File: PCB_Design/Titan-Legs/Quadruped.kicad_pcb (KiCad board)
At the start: 4 copper layers, 55.5 x 55.5 mm, 85 parts, among them IC1 TPS54260DGQR, IC2 CP2102, IC3 DRV8323RSRGZT, J1 TYPE-C-31-M-12, J2 691214110003, P1 282837-2, P2 282837-2, Q1 BSC031N06NS3GATMA1, Q2 BSC031N06NS3GATMA1, Q3 BSC031N06NS3GATMA1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

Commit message: Added Changes after First Review
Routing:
- net /DRV8323/MOTOR_A: track 27.0 -> 28.2 mm
- net Net-(C31-Pad2): track 21.4 -> 22.6 mm
- net /IO20: track 35.1 -> 34.1 mm
- net /DRV8323/SPB: track 19.2 -> 18.2 mm
- net /DRV8323/GLB: track 22.0 -> 22.9 mm
- net /IO8: track 26.9 -> 27.6 mm
- net /DRV8323/SPA: track 54.0 -> 53.6 mm, vias 3 -> 2
- net VM: vias 44 -> 69
- net GND: vias 46 -> 91
- added copper zone on B.Cu, net GND

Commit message: Added Changes after First Review
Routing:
- net VM: track 46.3 -> 52.2 mm, vias 69 -> 129
- net /RTS: track 54.8 -> 55.3 mm
- net GND: vias 91 -> 83
- added copper zone on In2.Cu, net /DRV8323/MOTOR_A
- added copper zone on In2.Cu, net /DRV8323/MOTOR_B
- added copper zone on In2.Cu, net /DRV8323/MOTOR_C

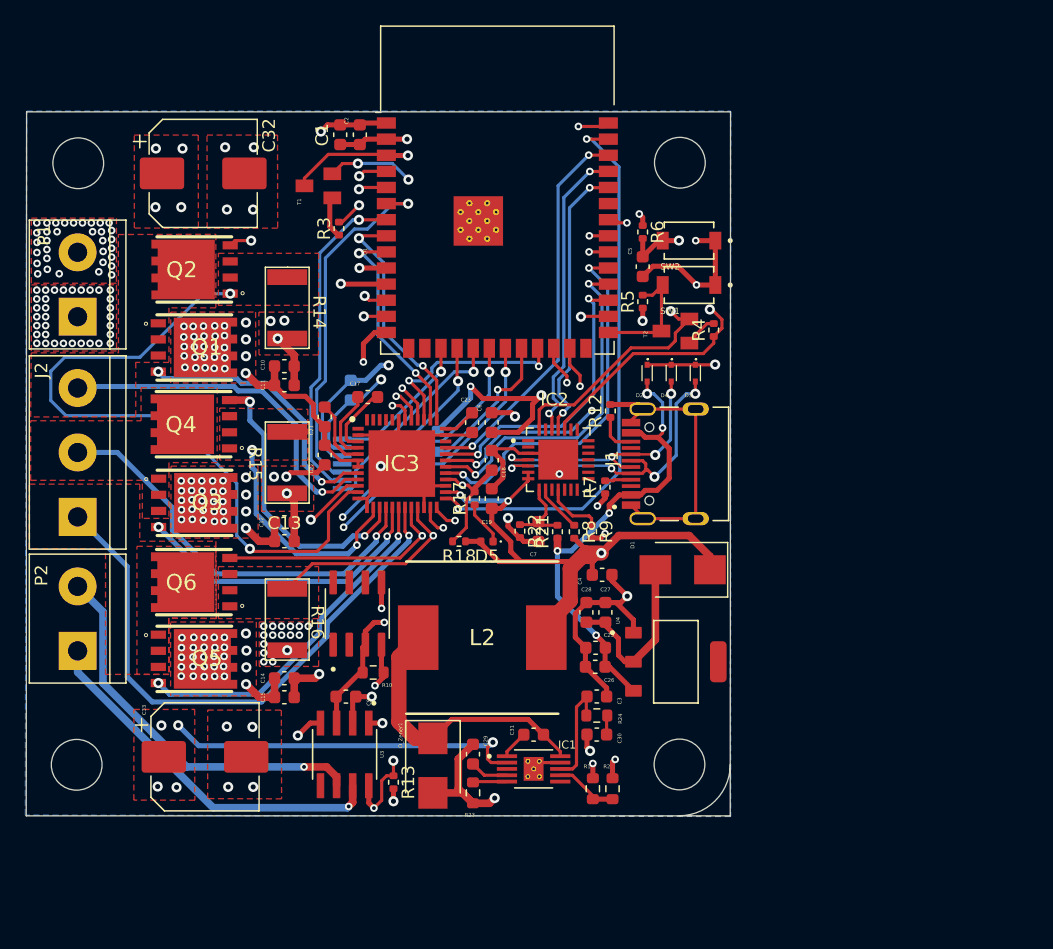
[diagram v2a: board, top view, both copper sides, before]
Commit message: Merged silkscreen changes and completed final prototype
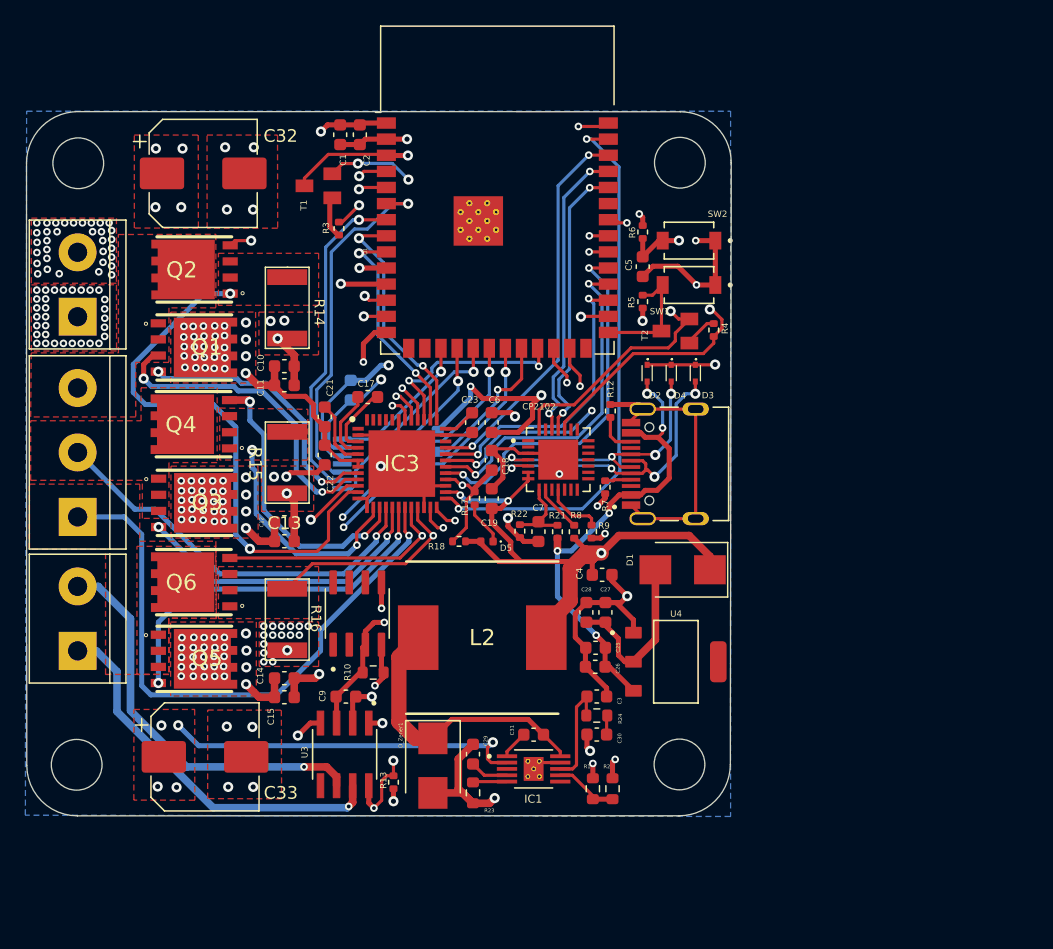
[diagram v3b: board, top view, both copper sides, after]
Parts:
- added G***: LOGO, LOGO, B.Cu at (64.5, 116.2)
- added G***: LOGO, LOGO, B.Cu at (64.1, 121.8)
- added G***: LOGO, LOGO, B.Cu at (47.6, 89.0)
- added G***: LOGO, LOGO, B.Cu at (70.1, 89.0)
- renumbered IC2 to CP2102
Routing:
- net /DRV8323/SPA: track 53.8 -> 43.3 mm
- net /DRV8323/MOTOR_A: track 28.2 -> 25.7 mm, vias 1 -> 2
- net /DRV8323/MOTOR_C: track 45.9 -> 47.7 mm
- net /DRV8323/GHC: track 27.6 -> 29.0 mm
- net /DRV8323/MOTOR_B: track 32.7 -> 31.6 mm
- net /CAN_BUS_IC/CANL: track 30.6 -> 31.6 mm
- net /CAN_BUS_IC/CANH: track 29.3 -> 30.2 mm
- net /IO4: track 40.8 -> 40.0 mm
- net /IO5: track 38.5 -> 37.7 mm
- net /DRV8323/GLA: track 31.1 -> 31.7 mm
- net VM: vias 129 -> 127
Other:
- board size 55.5 x 55.5 mm -> 55.6 x 55.5 mm
- board text added: "&"
- board text added: "Designed by"

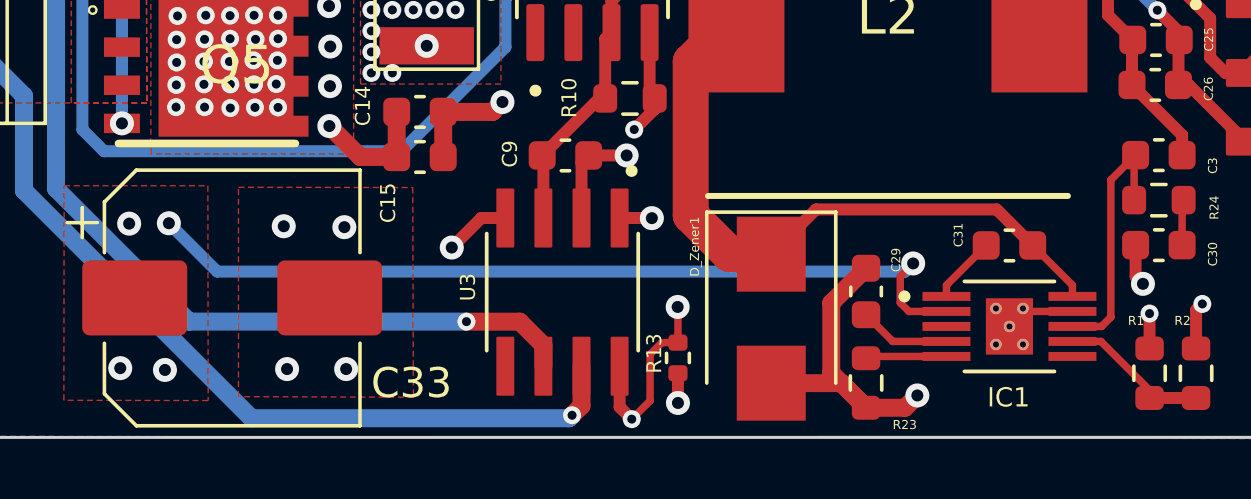
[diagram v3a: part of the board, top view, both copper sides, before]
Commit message: removed unnecessary files
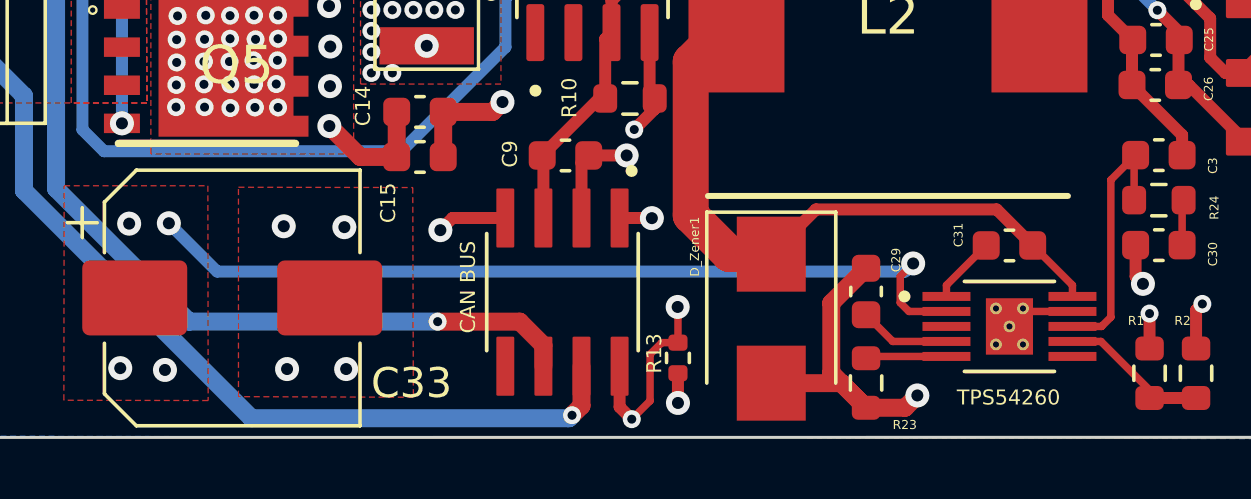
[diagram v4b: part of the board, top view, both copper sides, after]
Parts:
- CAN BUS: renamed from U3
- renumbered IC1 to TPS54260

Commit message: Merged the silkscreen MA,MB,MC and added vias in shunt resistors
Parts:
- removed C18: 0.1uF, Capacitor_SMD:C_0603_1608Metric
- added G***: LOGO, LOGO, B.Cu at (30.1, 97.2)
- added G***: LOGO, LOGO, B.Cu at (30.0, 102.3)
- added G***: LOGO, LOGO, B.Cu at (30.0, 112.9)
- added G***: LOGO, LOGO, B.Cu at (30.1, 107.2)
- added G***: LOGO, LOGO, B.Cu at (30.1, 117.8)
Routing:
- net GND: track 158.2 -> 151.6 mm, vias 83 -> 94
- net /IO47: track 26.7 -> 24.4 mm

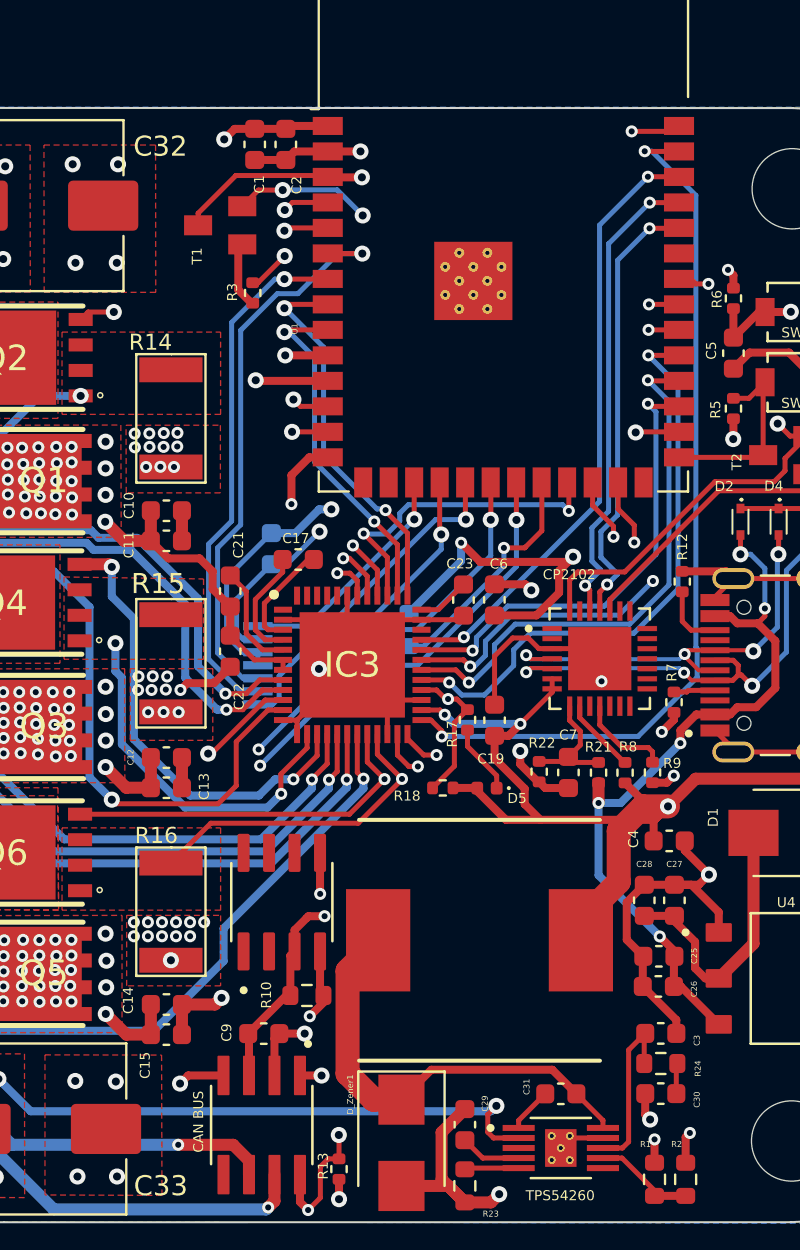
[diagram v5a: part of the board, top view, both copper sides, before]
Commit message: Merged the silkscreen MA,MB,MC and added more vias in shunt resistors
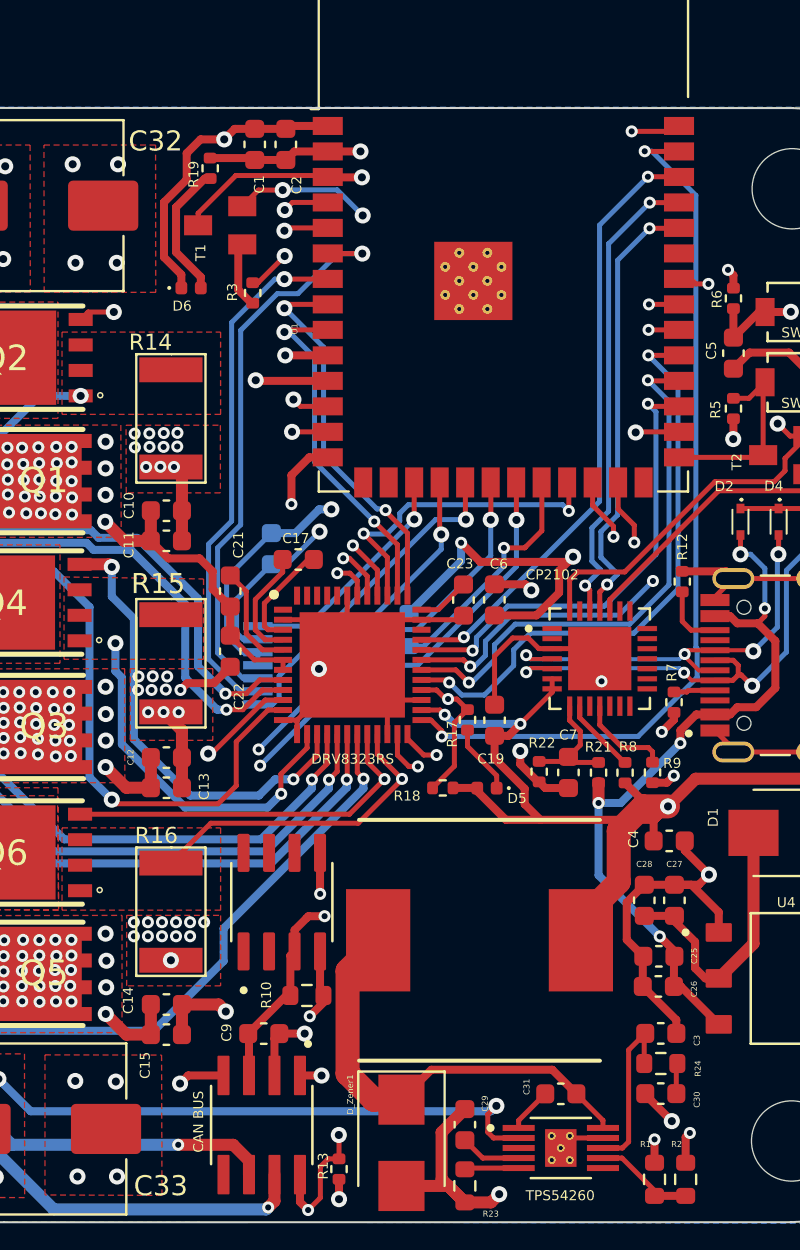
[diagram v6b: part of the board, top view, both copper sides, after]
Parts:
- added D6: LED, LED_SMD:LED_0402_1005Metric, F.Cu at (50.3, 84.3)
- added R19: 330, Resistor_SMD:R_0402_1005Metric, F.Cu at (51.3, 78.3)
- renumbered IC3 to DRV8323RS
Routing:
- net GND: track 151.6 -> 167.0 mm
- net Net-(D6-Pad2): track 0.00 -> 6.82 mm
- net 3V3_IN: track 98.5 -> 100.7 mm

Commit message: Added JLCPCB Logo on Back Silkscreen and final Changes Merged
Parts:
- added G***: LOGO, LOGO, B.Cu at (45.7, 79.8)
- moved G*** 20.6 mm to (66.0, 79.7)
- moved G*** 13.9 mm to (56.5, 91.3)
- moved G*** 0.92 mm to (64.8, 121.2)
- moved G*** 0.42 mm to (64.8, 116.0)

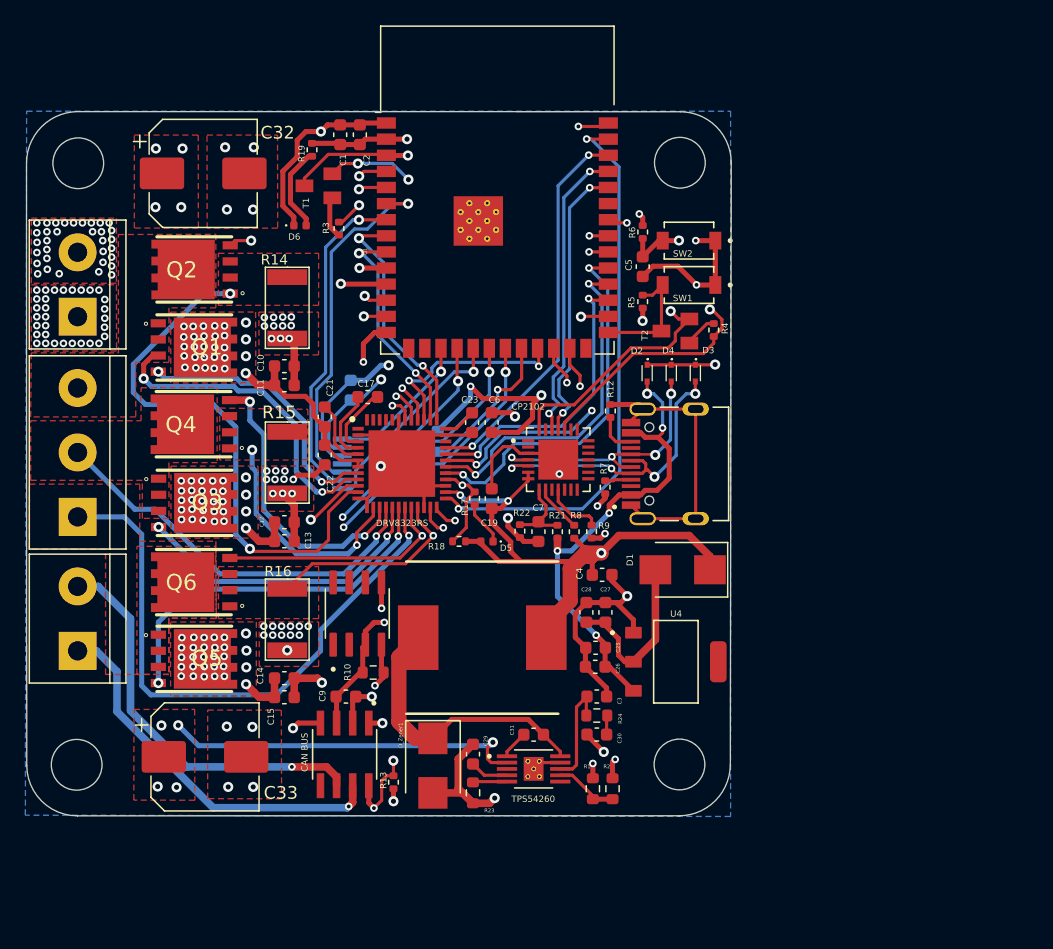
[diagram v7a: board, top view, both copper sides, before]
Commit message: Added Electrolytic Capacitor for TPS54260 and resisotrs for EN pin
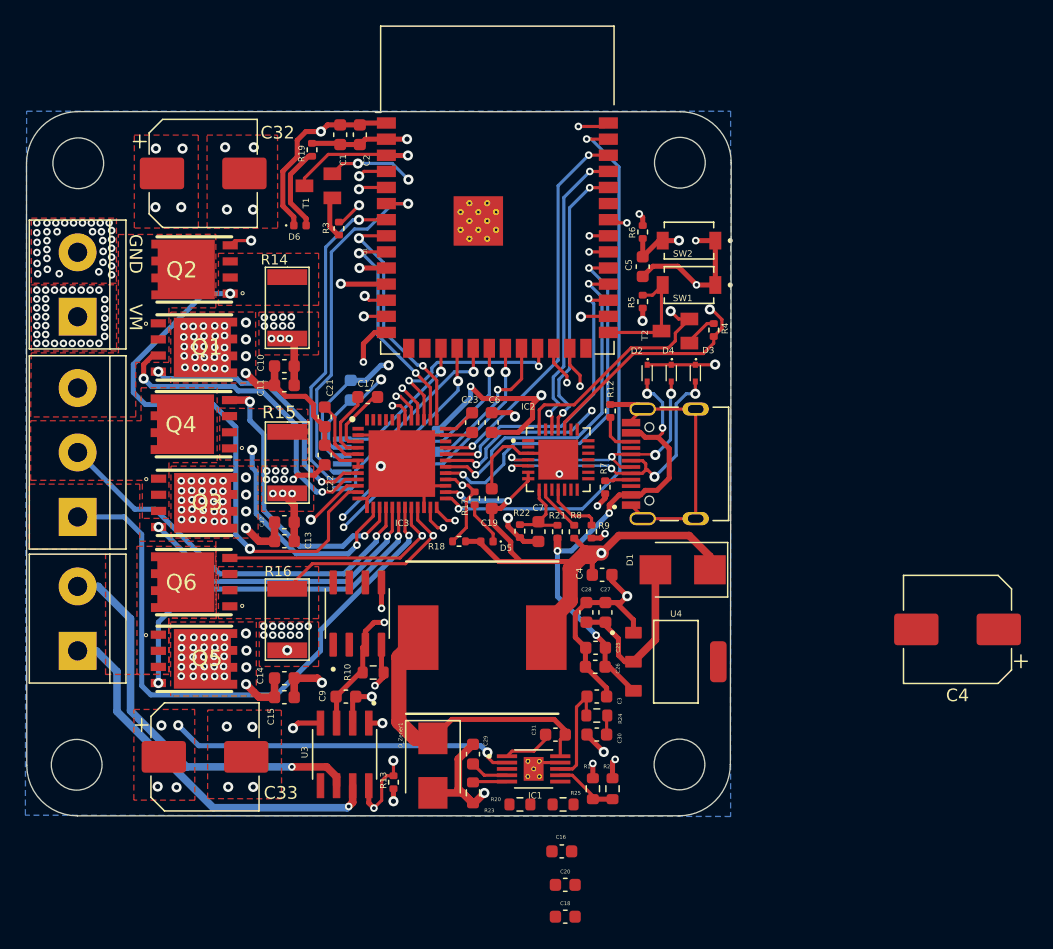
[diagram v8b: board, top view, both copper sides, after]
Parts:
- added C16: 2.2uF, Capacitor_SMD:C_0603_1608Metric, F.Cu at (71.0, 133.7)
- added C18: 2.2uF, Capacitor_SMD:C_0603_1608Metric, F.Cu at (71.2, 138.8)
- added C20: 2.2uF, Capacitor_SMD:C_0603_1608Metric, F.Cu at (71.2, 136.3)
- added C4: 270uF, Capacitor_SMD:CP_Elec_8x10, F.Cu at (102.2, 116.2)
- added R20: 100K, Resistor_SMD:R_0603_1608Metric, F.Cu at (67.7, 129.9)
- added R25: 4.42K, Resistor_SMD:R_0603_1608Metric, F.Cu at (71.1, 129.9)
- C3: value 62pF -> 18pF
- C30: value 4.7nF -> 2.2nF
- L2: value 47uH -> 22uH
- R23: value 1.37M -> 681K
- U3: renamed from CAN BUS
- moved C31 1.72 mm to (70.5, 124.5)
- renumbered TPS54260 to IC1, CP2102 to IC2, DRV8323RS to IC3
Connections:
- IC1 pad 12: GND -> (no net)
- IC1 pad 13: GND -> (no net)
- IC1 pad 14: GND -> (no net)
- IC1 pad 15: GND -> (no net)
- IC1 pad 16: GND -> (no net)
- IC1 pad 3: unconnected-(IC1-Pad3) -> /EN
- U1 pad 41: GND -> (no net)
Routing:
- net Net-(C31-Pad1): track 2.25 -> 3.97 mm
- net Net-(C31-Pad2): track 22.6 -> 24.1 mm
- net VM: track 52.2 -> 50.8 mm
- net GND: track 167.0 -> 166.4 mm
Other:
- board text added: "GND"
- board text added: "VM"
